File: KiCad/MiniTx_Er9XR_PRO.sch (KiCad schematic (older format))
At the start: 16 parts

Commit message: schematic adjustments
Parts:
- removed D? (x2): LED, symbol LED
- removed Q? (x3): Q_NMOS_DGS, symbol Q_NMOS_DGS
- removed R?: 300, symbol R_Small
- added C1, C2, C5: 470, Capacitors_SMD:C_0603_HandSoldering, symbol C_Small
- added C3, C4, C6, C7: 2.2uf, Capacitors_SMD:C_0603_HandSoldering, symbol C_Small
- added J1: CONN_01X03, Connectors:PINHEAD1-3, symbol CONN_01X03
- added J10, J6: LED2, Connectors:PINHEAD1-2, symbol CONN_01X02
- added J3: PWR2, Connectors:PINHEAD1-2, symbol CONN_01X02
- added J4: ENABLE2, Connectors:PINTST, symbol CONN_01X01
- added J5, J9: LED1, Connectors:PINHEAD1-2, symbol CONN_01X02
- added J7: MODULE1_POWER, Connectors:PINHEAD1-2, symbol CONN_01X02
- added J8: MODULE2_POWER, Connectors:PINHEAD1-2, symbol CONN_01X02
- added R1: 1K, Resistors_SMD:R_0603_HandSoldering, symbol R_Small
- added R3: 300, Resistors_SMD:R_0603_HandSoldering, symbol R_Small
- added R4, R5: 600, Resistors_SMD:R_0603_HandSoldering, symbol R_Small
- added U2, U3, U4: MIC5219-3.3BM5, TO_SOT_Packages_SMD:SOT-23-5, symbol MIC5219-3.3BM5
- R2, R6, R7, R8: renamed from R?; footprint (none) -> Resistors_SMD:R_0603_HandSoldering
- gave numbers to parts that had none: 6
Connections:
- net +3V3: now also SW2.1 (A), SW3.1 (A), C6.1, U4.5 (VOUT); no longer R2.1, R6.1, R7.1
- net CH5: now also R6.1, R7.1; no longer SW2.2 (B), SW3.2 (B)
- net GND: now also U1.14 (GND), C1.2, C2.2, C3.2, C4.2, C5.2, C6.2, C7.2, J1.2 (P2), J10.1 (P1), J3.1 (P1), J5.2 (P2), J6.2 (P2), J7.2 (P2), J8.2 (P2), J9.1 (P1), U2.2 (GND), U3.2 (GND), U4.2 (GND)
- net at U1.13 (RST): now also R1.1
- net at R6.2: now also SW2.2 (B), R4.1; no longer SW2.1 (A)
- net at R7.2: now also SW3.2 (B), R5.1; no longer SW3.1 (A)
- net at R2.2: now also J5.1 (P1)
- net POWER_MODULE1 renamed MODULE1_EN
- net POWER_MODULE2 renamed MODULE2_EN
- net POWER_TX renamed RESET_TX
- net RESET_TX: now also R1.2
- net VBAT renamed VBAT_SENSE
- new net: C3.1, J7.1 (P1), R2.1, U2.5 (VOUT)
- new net: C7.1, J1.3 (P3), U2.1 (VIN)
- new net: J1.1 (P1), U2.3 (EN)
- new net: C1.1, U2.4 (BYP)
- new net: C4.1, J8.1 (P1), R3.1, U3.5 (VOUT)
- new net: J6.1 (P1), R3.2
- new net: J3.2 (P2), U3.1 (VIN)
- new net: J4.1 (P1), U3.3 (EN)
- new net: C2.1, U3.4 (BYP)
- new net: C5.1, U4.4 (BYP)
- new net: J9.2 (P2), R4.2
- new net: J10.2 (P2), R5.2
- new net +BATT: U4.1 (VIN), U4.3 (EN)
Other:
- moved on the sheet: R2, R6, R7, SW3A

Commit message: Not sure how many changes
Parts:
- removed C4: 2.2uf, Capacitors_SMD:C_0603_HandSoldering, symbol C_Small
- removed J10: LED2, Connectors:PINHEAD1-2, symbol CONN_01X02
- removed J4: ENABLE2, Connectors:PINTST, symbol CONN_01X01
- removed J8: MODULE2_POWER, Connectors:PINHEAD1-2, symbol CONN_01X02
- removed R7: 5K, Resistors_SMD:R_0603_HandSoldering, symbol R_Small
- removed SW2: THRTL1, symbol SW_DPST_x2
- removed SW3: THRTL2, symbol SW_DPST_x2
- removed U3: MIC5219-3.3BM5, TO_SOT_Packages_SMD:SOT-23-5, symbol MIC5219-3.3BM5
- added J10: STAB, Connectors:PINHEAD1-3, symbol CONN_01X03
- added J11: CH5, Connectors:PINHEAD1-3, symbol CONN_01X03
- added J2: BAT2, Connectors:PINHEAD1-2, symbol CONN_01X02
- added J4: BAT, Connectors:PINHEAD1-2, symbol CONN_01X02
- added J8: 3.3V, Connectors:PINHEAD1-3, symbol CONN_01X03
- C2: value 470 -> 2.2uf
- J3: value PWR2 -> BAT1
- J6: value LED2 -> THRTL1
- R1: footprint Resistors_SMD:R_0603_HandSoldering -> (none)
- R3: value 300 -> 30K
- R5: value 600 -> 10K
- U1, U5: footprint DIL20 -> (none)
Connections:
- net +3V3: now also J10.1 (P1), J8.1 (P1), J8.2 (P2), J8.3 (P3)
- net +BATT: now also C2.1, J3.2 (P2), R3.1, J2.2 (P2), J4.2 (P2)
- net CH5: no longer R6.1, R8.1
- net GND: now also R5.2, J10.3 (P3), J11.3 (P3), J2.1 (P1), J4.1 (P1); no longer J6.2 (P2)
- net at R4.1, R6.2: now also J6.1 (P1)
- net at R5.1: now also R3.2, J10.2 (P2)
- new net: J11.2 (P2), R6.1, R8.1
- new net: J11.1 (P1), J6.2 (P2)
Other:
- note added: "3.3v"
- note added: "CH5"
- note added: "GND"
- note added: "V_SENSE"
- moved on the sheet: C5, C6, C7, J1, R8, SW1, U4

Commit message: Schematic values adjust
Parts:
- R3: value 30K -> 33K
- R4: value 600 -> 150
- R6: value 10K -> 10K/5.6K
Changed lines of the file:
@@
 P 6550 4650
 F 0 "R6" H 6580 4670 50  0000 L CNN
-F 1 "10K" H 6580 4610 50  0000 L CNN
+F 1 "10K/5.6K" V 6400 4500 50  0000 L CNN
 F 2 "Resistors_SMD:R_0603_HandSoldering" H 6550 4650 50  0001 C CNN
 F 3 "" H 6550 4650 50  0001 C CNN
@@
 P 6400 4950
 F 0 "R4" H 6430 4970 50  0000 L CNN
-F 1 "600" H 6430 4910 50  0000 L CNN
+F 1 "150" H 6430 4910 50  0000 L CNN
 F 2 "Resistors_SMD:R_0603_HandSoldering" H 6400 4950 50  0001 C CNN
 F 3 "" H 6400 4950 50  0001 C CNN
@@
 P 5250 2000
 F 0 "R3" H 5280 2020 50  0000 L CNN
-F 1 "30K" H 5280 1960 50  0000 L CNN
+F 1 "33K" H 5280 1960 50  0000 L CNN
 F 2 "Resistors_SMD:R_0603_HandSoldering" H 5250 2000 50  0001 C CNN
 F 3 "" H 5250 2000 50  0001 C CNN

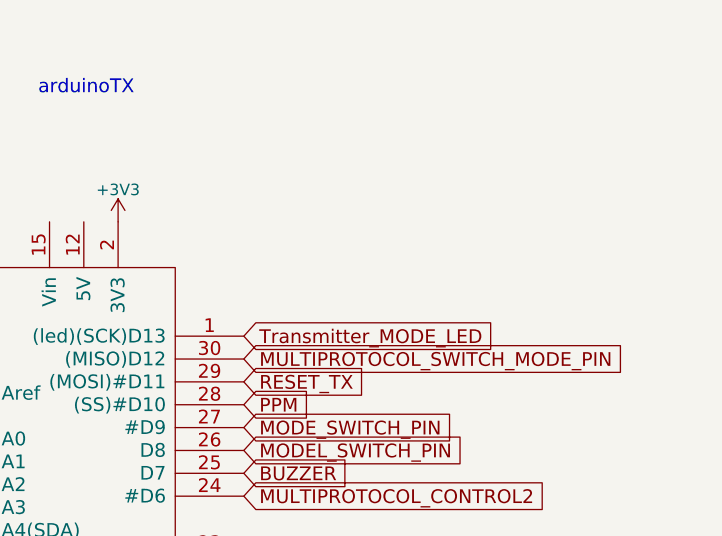
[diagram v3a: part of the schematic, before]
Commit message: openscad model and reduced one button
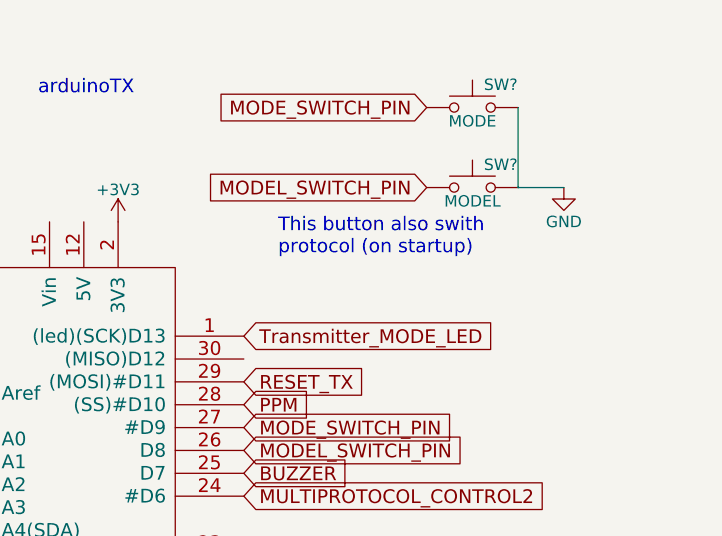
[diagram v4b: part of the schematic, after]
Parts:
- added SW?: MODE, symbol SW_Push
- added SW?: MODEL, symbol SW_Push
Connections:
- net GND: now also SW?.2, SW?.2
- net MODEL_SWITCH_PIN: now also SW?.1
- net MODE_SWITCH_PIN: now also SW?.1
- net MULTIPROTOCOL_SWITCH_MODE_PIN: no longer names the net of U5.30 ((MISO)D12)
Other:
- note added: "This button also swith \nprotocol (on startup)"
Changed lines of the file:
@@
 Text GLabel 8750 2400 2    60   Input ~ 0
 PPM
-Text GLabel 8750 2200 2    60   Input ~ 0
-MULTIPROTOCOL_SWITCH_MODE_PIN
 Text GLabel 8750 2100 2    60   Input ~ 0
 Transmitter_MODE_LED
@@
 Wire Wire Line
 	5050 1000 4850 1000
+$Comp
+L SW_Push SW?
+U 1 1 590B8035
+P 9750 1100
+F 0 "SW?" H 9800 1200 50  0000 L CNN
+F 1 "MODE" H 9750 1040 50  0000 C CNN
+F 2 "" H 9750 1300 50  0001 C CNN
+F 3 "" H 9750 1300 50  0001 C CNN
+	1    9750 1100
+	1    0    0    -1
+$EndComp
+$Comp
+L SW_Push SW?
+U 1 1 590B84BA
+P 9750 1450
+F 0 "SW?" H 9800 1550 50  0000 L CNN
+F 1 "MODEL" H 9750 1390 50  0000 C CNN
+F 2 "" H 9750 1650 50  0001 C CNN
+F 3 "" H 9750 1650 50  0001 C CNN
+	1    9750 1450
+	1    0    0    -1
+$EndComp
+Wire Wire Line
+	9950 1100 9950 1450
+$Comp
+L GND #PWR?
+U 1 1 590B8C35
+P 10150 1450
+F 0 "#PWR?" H 10150 1200 50  0001 C CNN
+F 1 "GND" H 10150 1300 50  0000 C CNN
+F 2 "" H 10150 1450 50  0001 C CNN
+F 3 "" H 10150 1450 50  0001 C CNN
+	1    10150 1450
+	1    0    0    -1
+$EndComp
+Wire Wire Line
+	9950 1450 10150 1450
+Text GLabel 9550 1100 0    60   Input ~ 0
+MODE_SWITCH_PIN
+Text GLabel 9550 1450 0    60   Input ~ 0
+MODEL_SWITCH_PIN
+Text Notes 8900 1750 0    60   ~ 0
+This button also swith \nprotocol (on startup)
 $EndSCHEMATC

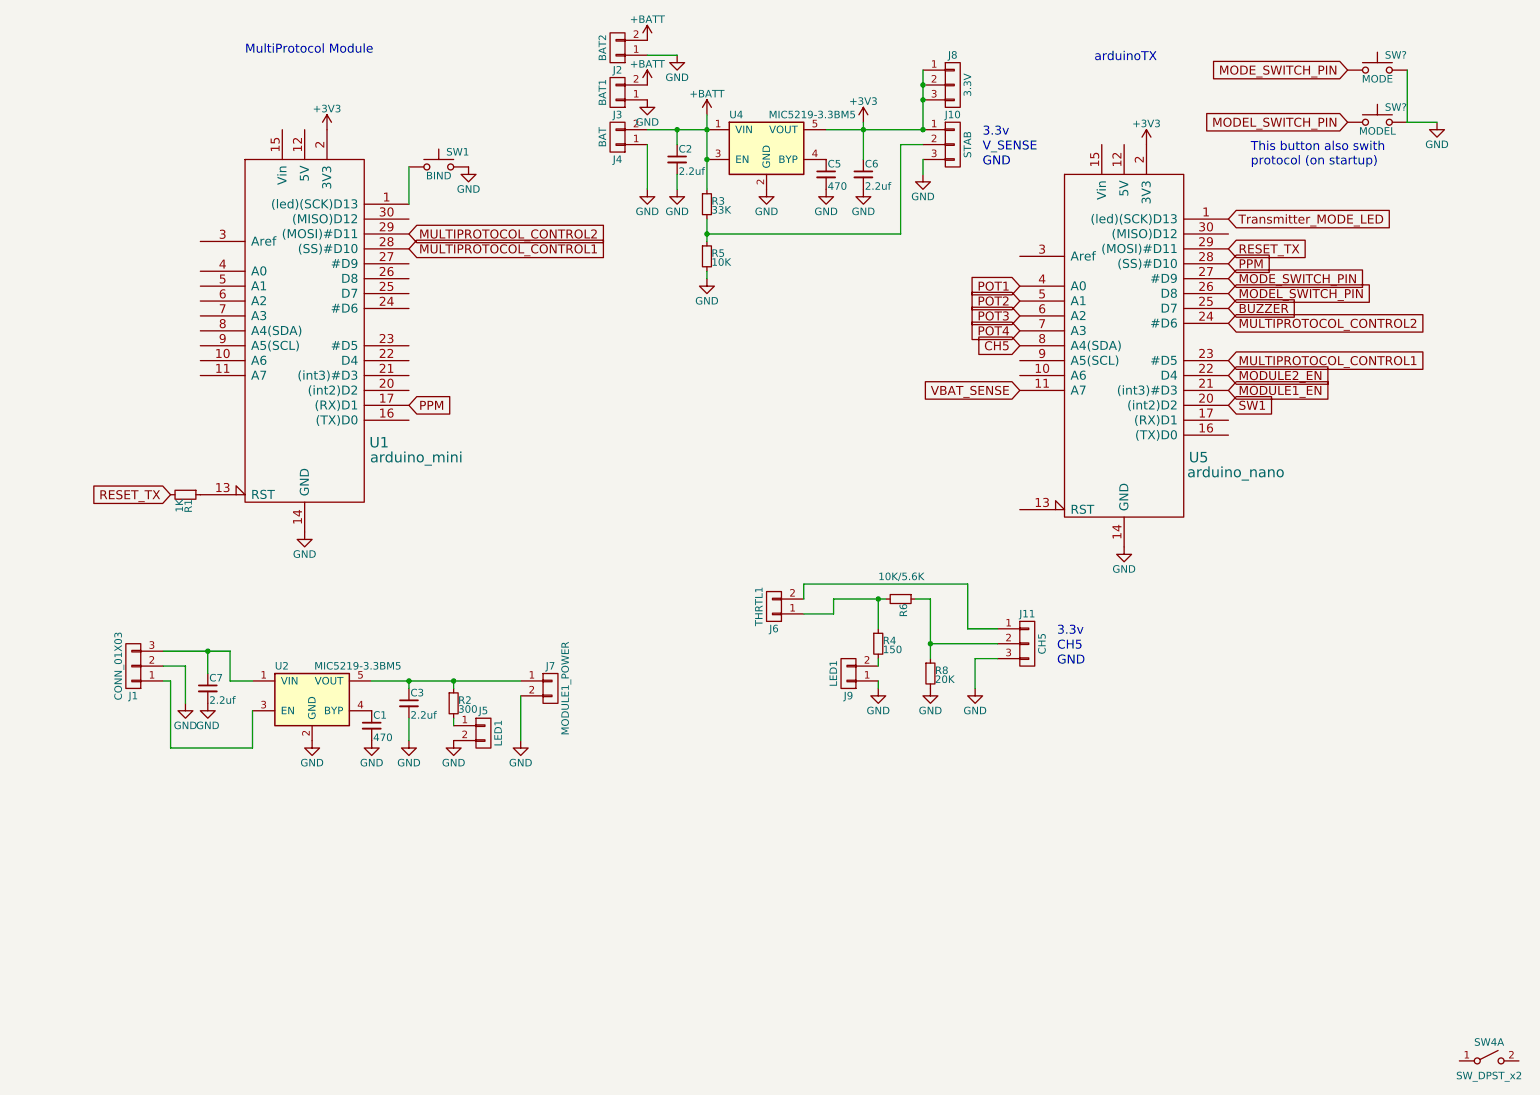
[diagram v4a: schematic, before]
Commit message: Adjust CH5 analog input, OpenSCAD, Schematic
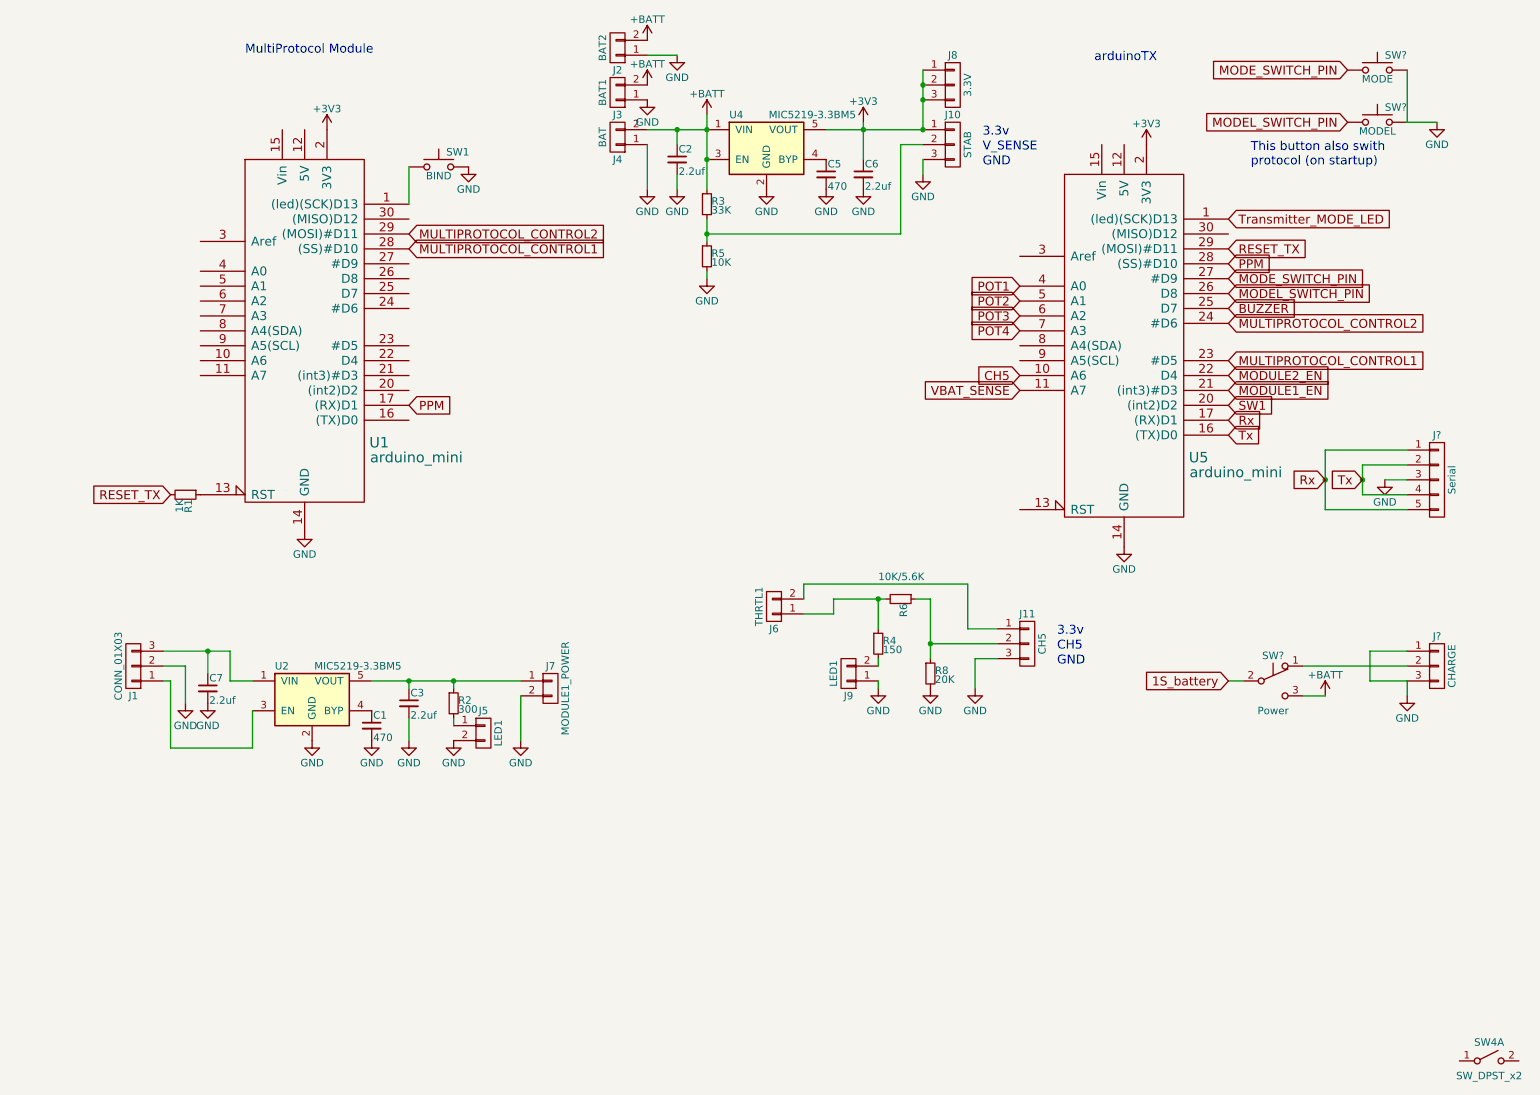
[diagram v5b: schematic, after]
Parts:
- added J?: CHARGE, symbol CONN_01X03
- added J?: Serial, symbol CONN_01X05
- added SW?: Power, symbol SW_Push_SPDT
- U5: value arduino_nano -> arduino_mini
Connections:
- net +BATT: now also SW?.3 (C)
- net CH5: now also U5.10 (A6); no longer U5.8 (A4(SDA))
- net GND: now also J?.1 (P1), J?.3 (P3), J?.3 (P3)
- net Tx: now reaches U5.16 ((TX)D0)
- net Tx: now also J?.2 (P2), J?.4 (P4)
- net Rx: now reaches U5.17 ((RX)D1)
- net Rx: now also J?.1 (P1), J?.5 (P5)
- new net: J?.2 (P2), SW?.1 (A)
- new net 1S_battery: SW?.2 (B)
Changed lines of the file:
@@
 P 8050 2750
 F 0 "U5" H 8550 1800 70  0000 C CNN
-F 1 "arduino_nano" H 8800 1700 70  0000 C CNN
+F 1 "arduino_mini" H 8800 1700 70  0000 C CNN
 F 2 "" H 8050 2700 60  0000 C CNN
 F 3 "" H 8050 2750 60  0001 C CNN
@@
 Text GLabel 7350 2850 0    60   Input ~ 0
 POT4
-Text GLabel 7350 2950 0    60   Input ~ 0
+Text GLabel 7350 3150 0    60   Input ~ 0
 CH5
 Text GLabel 8750 3350 2    60   Input ~ 0
@@
 $EndComp
 Wire Wire Line
-	6750 4650 6750 5050
+	6750 4650 6750 4950
+Wire Wire Line
+	6750 4950 6750 5050
 Connection ~ 6750 4950
 $Comp
@@
 $EndComp
 Wire Wire Line
-	3000 5200 4000 5200
+	3000 5200 3250 5200
+Wire Wire Line
+	3250 5200 3550 5200
+Wire Wire Line
+	3550 5200 4000 5200
 $Comp
 L GND #PWR010
@@
 $EndComp
 Wire Wire Line
-	5250 1400 5250 1900
-Wire Wire Line
-	6700 1500 6050 1500
+	5250 1400 5250 1500
+Wire Wire Line
+	5250 1500 5250 1700
+Wire Wire Line
+	5250 1700 5250 1900
+Wire Wire Line
+	6700 1500 6300 1500
+Wire Wire Line
+	6300 1500 6050 1500
 $Comp
 L CONN_01X02 J5
@@
 	6650 4650 6750 4650
 Wire Wire Line
-	6100 4650 6450 4650
+	6100 4650 6400 4650
+Wire Wire Line
+	6400 4650 6450 4650
 $Comp
 L CONN_01X02 J9
@@
 $EndComp
 Wire Wire Line
-	1600 5000 2050 5000
+	1600 5000 1900 5000
+Wire Wire Line
+	1900 5000 2050 5000
 Wire Wire Line
 	3550 5250 3550 5200
@@
 Connection ~ 5250 1700
 Wire Wire Line
-	5250 2100 5250 2250
+	5250 2100 5250 2200
+Wire Wire Line
+	5250 2200 5250 2250
 Wire Wire Line
 	5250 2500 5250 2450
@@
 $EndComp
 Wire Wire Line
-	4850 1500 5250 1500
+	4850 1500 5050 1500
+Wire Wire Line
+	5050 1500 5250 1500
 $Comp
 L GND #PWR022
@@
 Connection ~ 5250 1500
 Wire Wire Line
-	6300 1450 6300 1700
+	6300 1450 6300 1500
+Wire Wire Line
+	6300 1500 6300 1700
 Connection ~ 6300 1500
 $Comp
@@
 $EndComp
 Wire Wire Line
-	6700 1100 6700 1500
+	6700 1100 6700 1200
+Wire Wire Line
+	6700 1200 6700 1300
+Wire Wire Line
+	6700 1300 6700 1500
 Connection ~ 6700 1200
 Connection ~ 6700 1300
@@
 Text Notes 8900 1750 0    60   ~ 0
 This button also swith \nprotocol (on startup)
+$Comp
+L CONN_01X03 J?
+U 1 1 590C9AD0
+P 10150 5100
+F 0 "J?" H 10150 5300 50  0000 C CNN
+F 1 "CHARGE" V 10250 5100 50  0000 C CNN
+F 2 "" H 10150 5100 50  0001 C CNN
+F 3 "" H 10150 5100 50  0001 C CNN
+	1    10150 5100
+	1    0    0    -1
+$EndComp
+Wire Wire Line
+	9950 5000 9700 5000
+Wire Wire Line
+	9700 5000 9700 5200
+Wire Wire Line
+	9700 5200 9950 5200
+$Comp
+L GND #PWR?
+U 1 1 590CBAA3
+P 9950 5300
+F 0 "#PWR?" H 9950 5050 50  0001 C CNN
+F 1 "GND" H 9950 5150 50  0000 C CNN
+F 2 "" H 9950 5300 50  0001 C CNN
+F 3 "" H 9950 5300 50  0001 C CNN
+	1    9950 5300
+	1    0    0    -1
+$EndComp
+Wire Wire Line
+	9950 5200 9950 5300
+$Comp
+L SW_Push_SPDT SW?
+U 1 1 590CD79D
+P 9050 5200
+F 0 "SW?" H 9050 5370 50  0000 C CNN
+F 1 "Power" H 9050 5000 50  0000 C CNN
+F 2 "" H 9050 5200 50  0001 C CNN
+F 3 "" H 9050 5200 50  0001 C CNN
+	1    9050 5200
+	1    0    0    -1
+$EndComp
+$Comp
+L +BATT #PWR?
+U 1 1 590CE207
+P 9400 5300
+F 0 "#PWR?" H 9400 5150 50  0001 C CNN
+F 1 "+BATT" H 9400 5440 50  0000 C CNN
+F 2 "" H 9400 5300 50  0001 C CNN
+F 3 "" H 9400 5300 50  0001 C CNN
+	1    9400 5300
+	1    0    0    -1
+$EndComp
+Wire Wire Line
+	8750 5200 8850 5200
+Wire Wire Line
+	9250 5100 9950 5100
+Wire Wire Line
+	9250 5300 9400 5300
+Text GLabel 8750 5200 0    60   Input ~ 0
+1S_battery
+$Comp
+L CONN_01X05 J?
+U 1 1 590D4E0F
+P 10150 3850
+F 0 "J?" H 10150 4150 50  0000 C CNN
+F 1 "Serial" V 10250 3850 50  0000 C CNN
+F 2 "" H 10150 3850 50  0001 C CNN
+F 3 "" H 10150 3850 50  0001 C CNN
+	1    10150 3850
+	1    0    0    -1
+$EndComp
+Text GLabel 9400 3850 0    60   Input ~ 0
+Rx
+Text GLabel 9650 3850 0    60   Input ~ 0
+Tx
+$Comp
+L GND #PWR?
+U 1 1 590D5AD8
+P 9800 3850
+F 0 "#PWR?" H 9800 3600 50  0001 C CNN
+F 1 "GND" H 9800 3700 50  0000 C CNN
+F 2 "" H 9800 3850 50  0001 C CNN
+F 3 "" H 9800 3850 50  0001 C CNN
+	1    9800 3850
+	1    0    0    -1
+$EndComp
+Wire Wire Line
+	9950 3850 9800 3850
+Text GLabel 8750 3450 2    60   Input ~ 0
+Rx
+Text GLabel 8750 3550 2    60   Input ~ 0
+Tx
+Wire Wire Line
+	9950 3750 9650 3750
+Wire Wire Line
+	9650 3750 9650 3850
+Wire Wire Line
+	9650 3850 9650 3950
+Wire Wire Line
+	9650 3950 9950 3950
+Wire Wire Line
+	9950 4050 9400 4050
+Wire Wire Line
+	9400 4050 9400 3850
+Wire Wire Line
+	9400 3850 9400 3650
+Wire Wire Line
+	9400 3650 9950 3650
+Connection ~ 9650 3850
+Connection ~ 9400 3850
 $EndSCHEMATC

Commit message: led resistor to 39 ohm
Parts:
- R2: value 300 -> 39
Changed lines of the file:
@@
 P 3550 5350
 F 0 "R2" H 3580 5370 50  0000 L CNN
-F 1 "300" H 3580 5310 50  0000 L CNN
+F 1 "39" H 3580 5310 50  0000 L CNN
 F 2 "Resistors_SMD:R_0603_HandSoldering" H 3550 5350 50  0001 C CNN
 F 3 "" H 3550 5350 50  0001 C CNN
